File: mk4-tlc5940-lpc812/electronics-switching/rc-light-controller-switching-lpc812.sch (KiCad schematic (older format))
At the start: 20 parts, among them J1 Pinheader right-angle 2x17, J2 Pinheader straight 1x06, J3 Pinheader straight 1x06, T1 PMV30UN, T2 PMV30UN, T3 PMV30UN, T4 PMV30UN, T5 PMV30UN, T6 PMV30UN, T7 PMV30UN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

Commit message: Tweak schematics, layout text and add BOM CSV files
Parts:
- U2: value 3V3 -> MCP1703A-3302_SOT23
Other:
- moved on the sheet: C1, C2, C3, J1, J2, J3, RN1, T1, T2, T3, T4, T5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

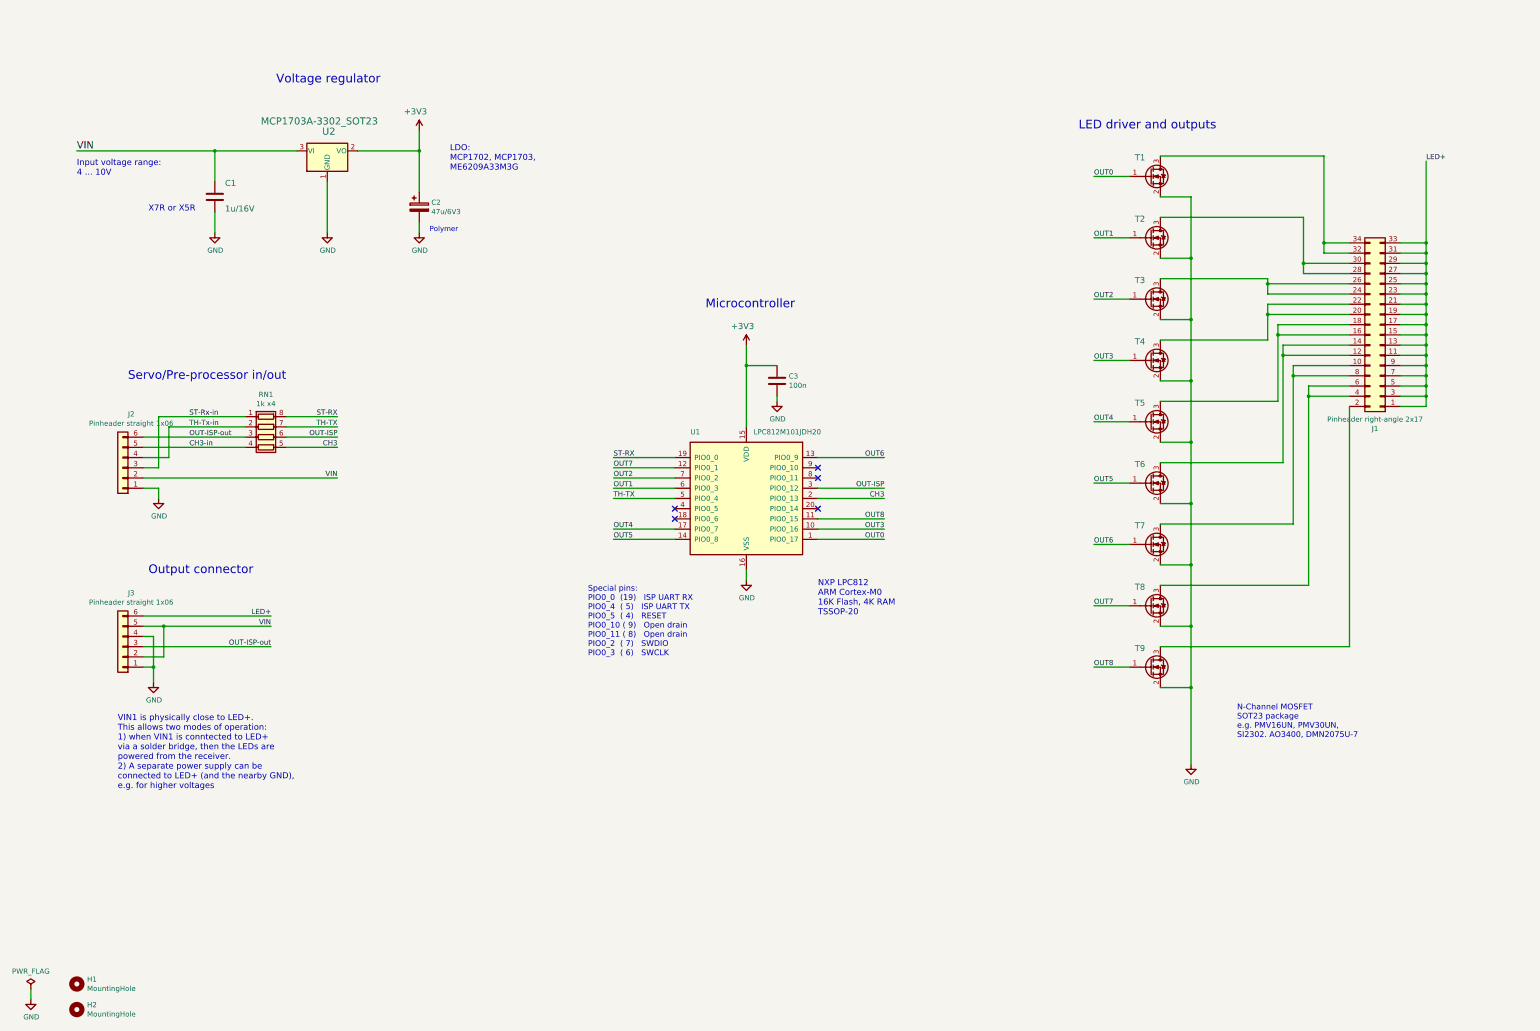
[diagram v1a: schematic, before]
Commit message: Swap VIN and LED+, add version detection
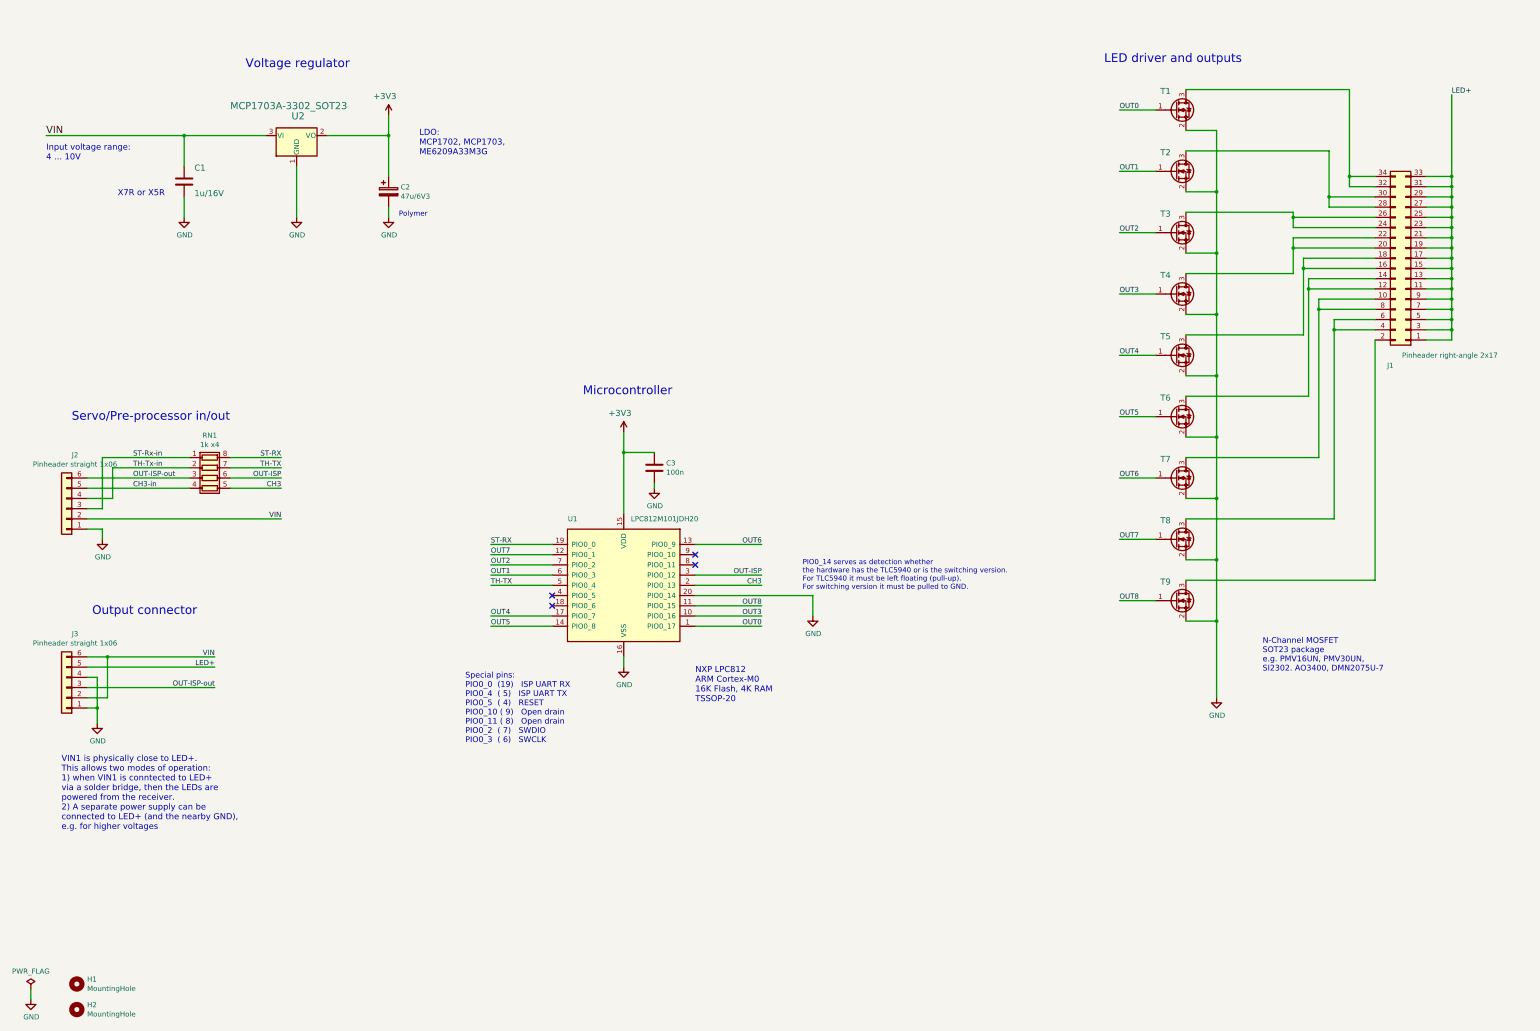
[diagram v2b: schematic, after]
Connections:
- net GND: now also U1.20 (PIO0_14)
- net LED+: now also J3.5 (Pin_5); no longer J3.6 (Pin_6)
- net VIN: now also J3.6 (Pin_6); no longer J3.5 (Pin_5)
- no-connect marks 5 -> 4
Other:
- note added: "PIO0_14 serves as detection whether \nthe hardware has the TLC5940 or is the switching version. \nFor TLC5940 it must be left floating (pull-up).\nFor switching version it must be pulled to GND."
- moved on the sheet: C1, C2, C3, J1, J2, J3, RN1, T1, T2, T3, T4, T5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

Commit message: Update text regarding jumper use
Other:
- note added: "VIN1 is physically close to LED+.\nThis allows two modes of operation:\n1) when VIN1 is conntected to LED+\nvia a jumper, then the LEDs are \npowered from the receiver.\n2) A separate power supply can be \nconnected to LED+ (and the nearby GND),\ne.g. for higher voltages"
- note removed: "VIN1 is physically close to LED+.\nThis allows two modes of operation:\n1) when VIN1 is conntected to LED+\nvia a solder bridge, then the LEDs are \npowered from the receiver.\n2) A separate power supply can be \nconnected to LED+ (and the nearby GND),\ne.g. for higher voltages"
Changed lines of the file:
@@
 	12450 2850 13500 2850
 Text Notes 1450 8900 0    59   ~ 0
-VIN1 is physically close to LED+.\nThis allows two modes of operation:\n1) when VIN1 is conntected to LED+\nvia a solder bridge, then the LEDs are \npowered from the receiver.\n2) A separate power supply can be \nconnected to LED+ (and the nearby GND),\ne.g. for higher voltages
+VIN1 is physically close to LED+.\nThis allows two modes of operation:\n1) when VIN1 is conntected to LED+\nvia a jumper, then the LEDs are \npowered from the receiver.\n2) A separate power supply can be \nconnected to LED+ (and the nearby GND),\ne.g. for higher voltages
 Text Notes 1750 6800 0    85   ~ 0
 Output connector
